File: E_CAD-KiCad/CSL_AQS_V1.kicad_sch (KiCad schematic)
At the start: 10 parts, among them J2 Grove STEMMA, J3 Grove STEMMA

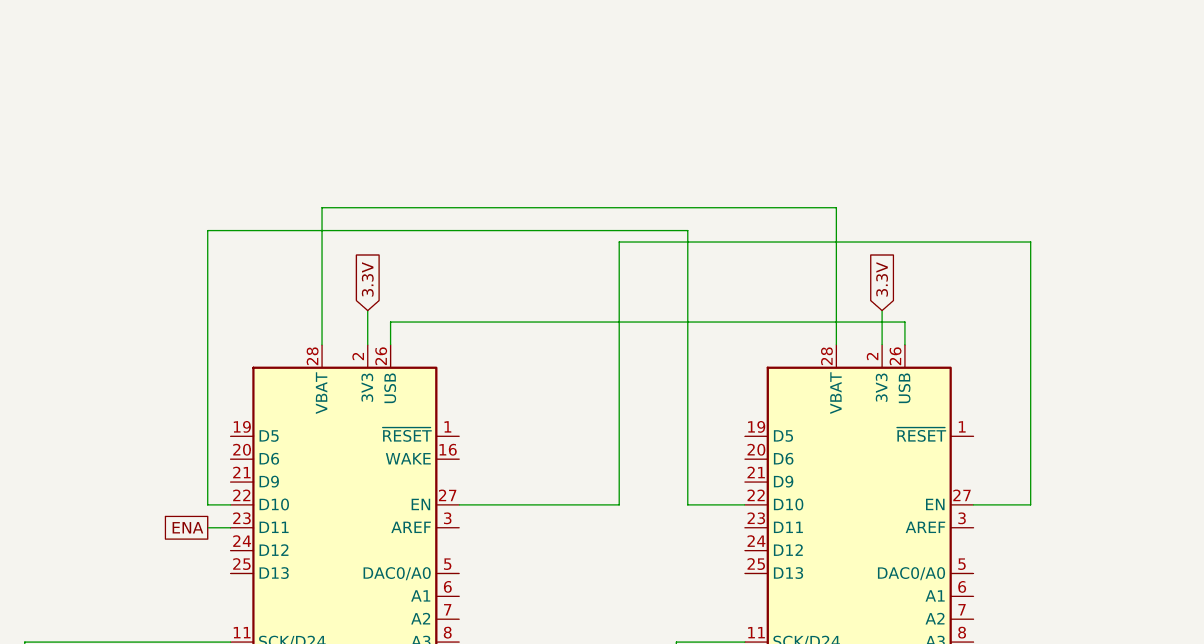
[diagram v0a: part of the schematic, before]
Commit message: Corrections to PCB
Corrections to component connections involving SCL and SDA
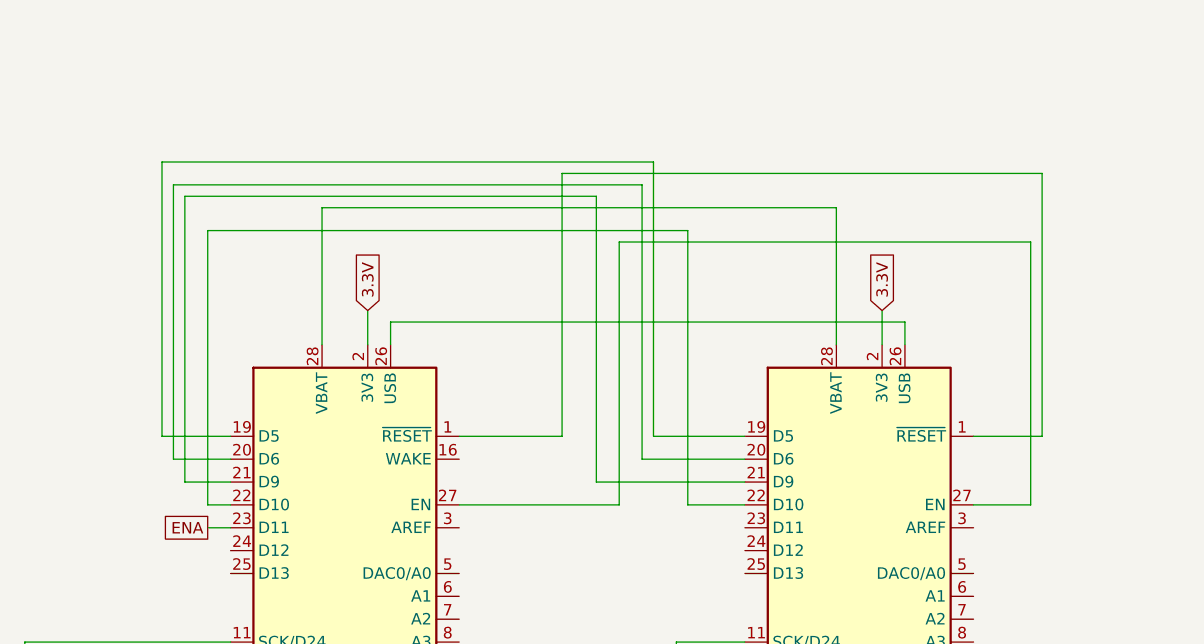
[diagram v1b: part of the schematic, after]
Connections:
- net at A1.1 (~{RESET}): now also A2.1 (~{RESET})
- net at A1.19 (D5): now also A2.19 (D5)
- net at A1.20 (D6): now also A2.20 (D6)
- net at A1.21 (D9): now also A2.21 (D9)
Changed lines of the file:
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@@
+	(wire
+		(pts
+			(xy 139.7 69.85) (xy 149.86 69.85)
+		)
+		(stroke
+			(width 0)
+			(type default)
+		)
+	)
+	(wire
+		(pts
+			(xy 133.35 43.18) (xy 133.35 74.93)
+		)
+		(stroke
+			(width 0)
+			(type default)
+		)
+	)
 	(wire
 		(pts
@@
 	(wire
 		(pts
+			(xy 182.88 40.64) (xy 182.88 69.85)
+		)
+		(stroke
+			(width 0)
+			(type default)
+		)
+	)
+	(wire
+		(pts
 			(xy 91.44 175.26) (xy 93.98 175.26)
 		)
@@
 	(wire
 		(pts
+			(xy 129.54 40.64) (xy 182.88 40.64)
+		)
+		(stroke
+			(width 0)
+			(type default)
+		)
+	)
+	(wire
+		(pts
 			(xy 30.48 148.59) (xy 35.56 148.59)
 		)
@@
 	(wire
 		(pts
+			(xy 87.63 43.18) (xy 133.35 43.18)
+		)
+		(stroke
+			(width 0)
+			(type default)
+		)
+	)
+	(wire
+		(pts
+			(xy 129.54 69.85) (xy 129.54 40.64)
+		)
+		(stroke
+			(width 0)
+			(type default)
+		)
+	)
+	(wire
+		(pts
 			(xy 30.48 124.46) (xy 36.83 124.46)
 		)
@@
 	(wire
 		(pts
+			(xy 138.43 72.39) (xy 149.86 72.39)
+		)
+		(stroke
+			(width 0)
+			(type default)
+		)
+	)
+	(wire
+		(pts
 			(xy 30.48 151.13) (xy 35.56 151.13)
 		)
@@
 	(wire
 		(pts
+			(xy 85.09 69.85) (xy 85.09 39.37)
+		)
+		(stroke
+			(width 0)
+			(type default)
+		)
+	)
+	(wire
+		(pts
 			(xy 160.02 59.69) (xy 160.02 44.45)
 		)
@@
 	(wire
 		(pts
+			(xy 118.11 69.85) (xy 129.54 69.85)
+		)
+		(stroke
+			(width 0)
+			(type default)
+		)
+	)
+	(wire
+		(pts
+			(xy 182.88 69.85) (xy 175.26 69.85)
+		)
+		(stroke
+			(width 0)
+			(type default)
+		)
+	)
+	(wire
+		(pts
 			(xy 88.9 113.03) (xy 92.71 113.03)
 		)
@@
 	(wire
 		(pts
+			(xy 87.63 74.93) (xy 87.63 43.18)
+		)
+		(stroke
+			(width 0)
+			(type default)
+		)
+	)
+	(wire
+		(pts
 			(xy 165.1 55.88) (xy 165.1 59.69)
 		)
@@
 	(wire
 		(pts
+			(xy 139.7 39.37) (xy 139.7 69.85)
+		)
+		(stroke
+			(width 0)
+			(type default)
+		)
+	)
+	(wire
+		(pts
 			(xy 91.44 177.8) (xy 93.98 177.8)
 		)
@@
 	(wire
 		(pts
+			(xy 138.43 41.91) (xy 138.43 72.39)
+		)
+		(stroke
+			(width 0)
+			(type default)
+		)
+	)
+	(wire
+		(pts
 			(xy 135.89 48.26) (xy 181.61 48.26)
 		)
@@
 	(wire
 		(pts
+			(xy 86.36 72.39) (xy 86.36 41.91)
+		)
+		(stroke
+			(width 0)
+			(type default)
+		)
+	)
+	(wire
+		(pts
+			(xy 92.71 74.93) (xy 87.63 74.93)
+		)
+		(stroke
+			(width 0)
+			(type default)
+		)
+	)
+	(wire
+		(pts
 			(xy 30.48 121.92) (xy 36.83 121.92)
 		)
@@
 	(wire
 		(pts
+			(xy 133.35 74.93) (xy 149.86 74.93)
+		)
+		(stroke
+			(width 0)
+			(type default)
+		)
+	)
+	(wire
+		(pts
 			(xy 73.66 137.16) (xy 144.78 137.16)
 		)
@@
 	(wire
 		(pts
+			(xy 85.09 39.37) (xy 139.7 39.37)
+		)
+		(stroke
+			(width 0)
+			(type default)
+		)
+	)
+	(wire
+		(pts
 			(xy 167.64 59.69) (xy 167.64 57.15)
 		)
@@
 	(wire
 		(pts
+			(xy 92.71 72.39) (xy 86.36 72.39)
+		)
+		(stroke
+			(width 0)
+			(type default)
+		)
+	)
+	(wire
+		(pts
 			(xy 38.1 77.47) (xy 41.91 77.47)
 		)
@@
 	(wire
 		(pts
+			(xy 92.71 69.85) (xy 85.09 69.85)
+		)
+		(stroke
+			(width 0)
+			(type default)
+		)
+	)
+	(wire
+		(pts
 			(xy 92.71 95.25) (xy 73.66 95.25)
 		)
@@
 		)
 		(stroke
+			(width 0)
+			(type default)
+		)
+	)
+	(wire
+		(pts
+			(xy 86.36 41.91) (xy 138.43 41.91)
+		)
+		(stroke
